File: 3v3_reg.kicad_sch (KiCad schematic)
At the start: 1 part, among them U7 TPS62A01PDDCR

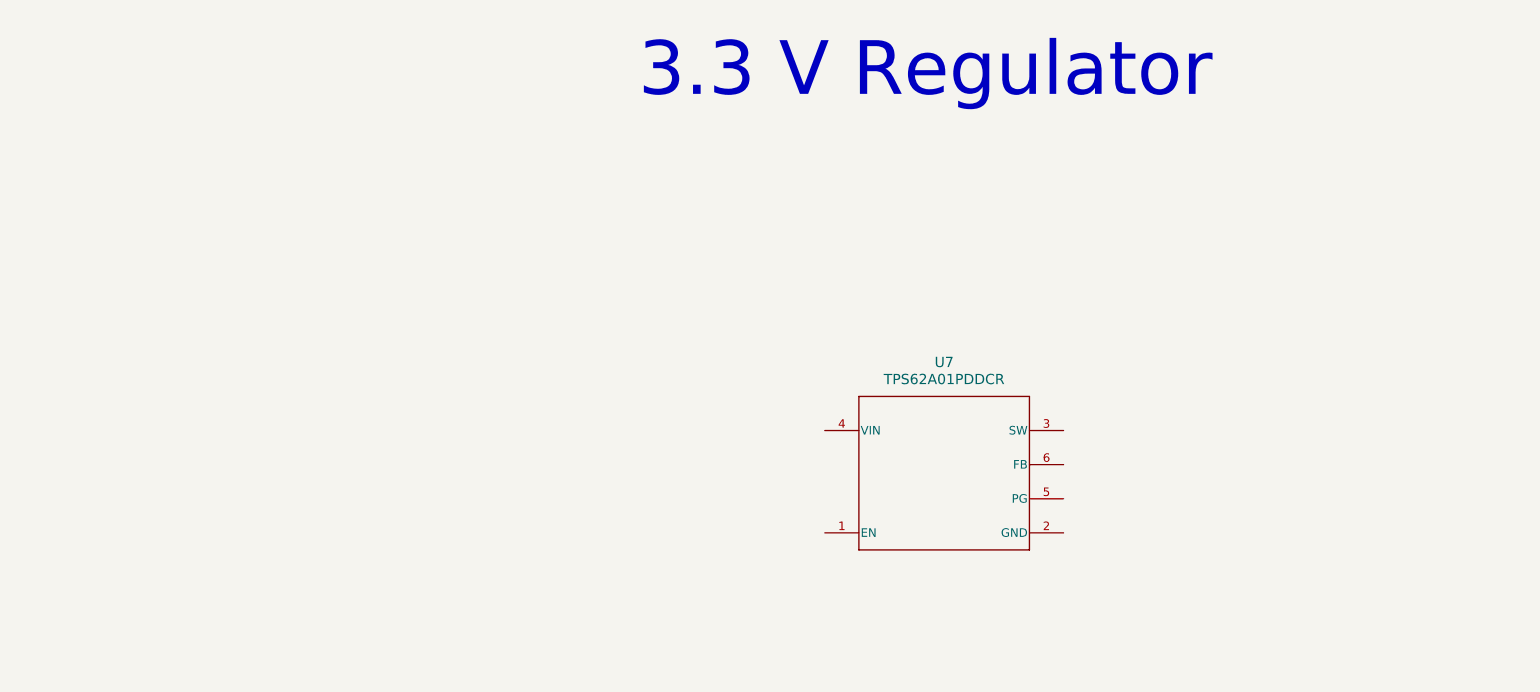
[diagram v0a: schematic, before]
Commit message: did 3v3 reg
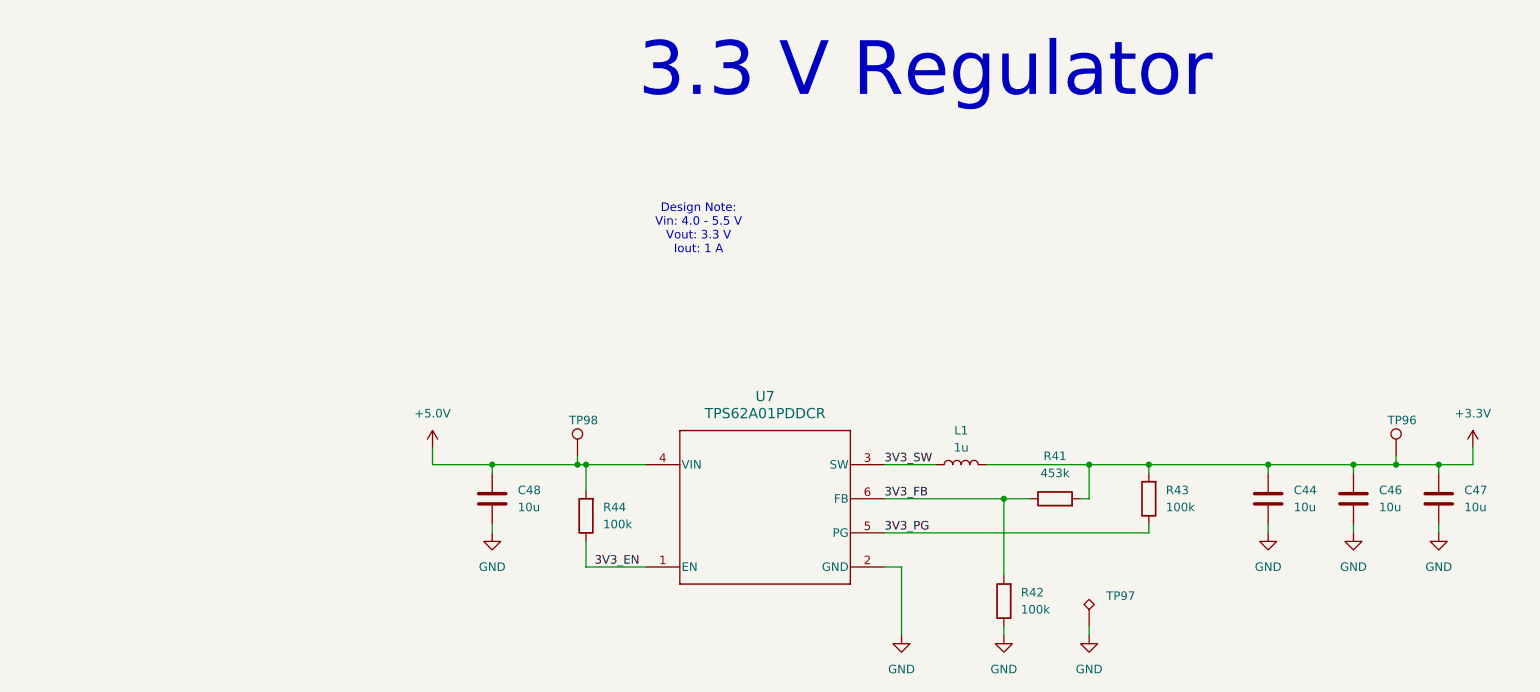
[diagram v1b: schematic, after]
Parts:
- added C44, C46, C47, C48: 10u, Capacitor_SMD:C_0805_2012Metric, symbol Device:C
- added L1: 1u, Inductor_SMD:L_1210_3225Metric, symbol Device:L
- added R41: 453k, Resistor_SMD:R_0402_1005Metric, symbol Device:R
- added R42, R43, R44: 100k, Resistor_SMD:R_0402_1005Metric, symbol Device:R
- added TP96, TP98: TestPoint, symbol Connector:TestPoint
- added TP97: TestPoint_Alt, symbol Connector:TestPoint_Alt
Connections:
- net 3V3_EN: now reaches U7.1 (EN)
- net 3V3_EN: now also R44.1
- net GND: now reaches U7.2 (GND)
- net GND: now also C44.2, C46.2, C47.2, C48.2, R42.1, TP97.1
- net 3V3_SW: now reaches U7.3 (SW)
- net 3V3_SW: now also L1.1
- net +5.0V: now reaches U7.4 (VIN)
- net +5.0V: now also C48.1, R44.2, TP98.1
- net 3V3_PG: now reaches U7.5 (PG)
- net 3V3_PG: now also R43.1
- net 3V3_FB: now reaches U7.6 (FB)
- net 3V3_FB: now also R41.1, R42.2
- new net +3.3V: C44.1, C46.1, C47.1, L1.2, R41.2, R43.2, TP96.1
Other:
- note added: "Design Note: Vin: 4.0 - 5.5 V Vout: 3.3 V Iout: 1 A"
- moved on the sheet: U7

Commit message: did stuff
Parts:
- renumbered C48 to C109, C44 to C110, C46 to C111, C47 to C112, R41 to R80, R43 to R81, R44 to R82, R42 to R83, TP98 to TP133, TP96 to TP134, TP97 to TP135
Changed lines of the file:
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@@
 		(dnp no)
 		(fields_autoplaced yes)
-		(property "Reference" "C44"
+		(property "Reference" "C110"
 			(at 199.39 96.5199 0)
 			(effects
@@
 			(project ""
 				(path "/2970f661-65ab-4e2b-aeda-d76d1044f2b8/4a874178-a54c-4eb4-8350-ff261e3dfdab"
-					(reference "C44")
+					(reference "C110")
 					(unit 1)
 				)
@@
 		(dnp no)
 		(fields_autoplaced yes)
-		(property "Reference" "R44"
+		(property "Reference" "R82"
 			(at 96.52 99.0599 0)
 			(effects
@@
 			(project "netdaq"
 				(path "/2970f661-65ab-4e2b-aeda-d76d1044f2b8/4a874178-a54c-4eb4-8350-ff261e3dfdab"
-					(reference "R44")
+					(reference "R82")
 					(unit 1)
 				)
@@
 		(dnp no)
 		(fields_autoplaced yes)
-		(property "Reference" "#PWR086"
+		(property "Reference" "#PWR0179"
 			(at 226.06 93.98 0)
 			(effects
@@
 			(project ""
 				(path "/2970f661-65ab-4e2b-aeda-d76d1044f2b8/4a874178-a54c-4eb4-8350-ff261e3dfdab"
-					(reference "#PWR086")
+					(reference "#PWR0179")
 					(unit 1)
 				)
@@
 		(dnp no)
 		(fields_autoplaced yes)
-		(property "Reference" "#PWR085"
+		(property "Reference" "#PWR0183"
 			(at 220.98 109.22 0)
 			(effects
@@
 			(project "netdaq"
 				(path "/2970f661-65ab-4e2b-aeda-d76d1044f2b8/4a874178-a54c-4eb4-8350-ff261e3dfdab"
-					(reference "#PWR085")
+					(reference "#PWR0183")
 					(unit 1)
 				)
@@
 		(dnp no)
 		(fields_autoplaced yes)
-		(property "Reference" "#PWR088"
+		(property "Reference" "#PWR0180"
 			(at 80.01 109.22 0)
 			(effects
@@
 			(project "netdaq"
 				(path "/2970f661-65ab-4e2b-aeda-d76d1044f2b8/4a874178-a54c-4eb4-8350-ff261e3dfdab"
-					(reference "#PWR088")
+					(reference "#PWR0180")
 					(unit 1)
 				)
@@
 		(dnp no)
 		(fields_autoplaced yes)
-		(property "Reference" "#PWR089"
+		(property "Reference" "#PWR0178"
 			(at 71.12 93.98 0)
 			(effects
@@
 			(project "netdaq"
 				(path "/2970f661-65ab-4e2b-aeda-d76d1044f2b8/4a874178-a54c-4eb4-8350-ff261e3dfdab"
-					(reference "#PWR089")
+					(reference "#PWR0178")
 					(unit 1)
 				)
@@
 		(dnp no)
 		(fields_autoplaced yes)
-		(property "Reference" "#PWR087"
+		(property "Reference" "#PWR0186"
 			(at 168.91 124.46 0)
 			(effects
@@
 			(project "netdaq"
 				(path "/2970f661-65ab-4e2b-aeda-d76d1044f2b8/4a874178-a54c-4eb4-8350-ff261e3dfdab"
-					(reference "#PWR087")
+					(reference "#PWR0186")
 					(unit 1)
 				)
@@
 		(on_board yes)
 		(dnp no)
-		(property "Reference" "TP98"
+		(property "Reference" "TP133"
 			(at 91.44 86.106 0)
 			(effects
@@
 			(project "netdaq"
 				(path "/2970f661-65ab-4e2b-aeda-d76d1044f2b8/4a874178-a54c-4eb4-8350-ff261e3dfdab"
-					(reference "TP98")
+					(reference "TP133")
 					(unit 1)
 				)
@@
 		(dnp no)
 		(fields_autoplaced yes)
-		(property "Reference" "#PWR082"
+		(property "Reference" "#PWR0185"
 			(at 156.21 124.46 0)
 			(effects
@@
 			(project "netdaq"
 				(path "/2970f661-65ab-4e2b-aeda-d76d1044f2b8/4a874178-a54c-4eb4-8350-ff261e3dfdab"
-					(reference "#PWR082")
+					(reference "#PWR0185")
 					(unit 1)
 				)
@@
 		(dnp no)
 		(fields_autoplaced yes)
-		(property "Reference" "#PWR081"
+		(property "Reference" "#PWR0184"
 			(at 140.97 124.46 0)
 			(effects
@@
 			(project ""
 				(path "/2970f661-65ab-4e2b-aeda-d76d1044f2b8/4a874178-a54c-4eb4-8350-ff261e3dfdab"
-					(reference "#PWR081")
+					(reference "#PWR0184")
 					(unit 1)
 				)
@@
 		(dnp no)
 		(fields_autoplaced yes)
-		(property "Reference" "C46"
+		(property "Reference" "C111"
 			(at 212.09 96.5199 0)
 			(effects
@@
 			(project "netdaq"
 				(path "/2970f661-65ab-4e2b-aeda-d76d1044f2b8/4a874178-a54c-4eb4-8350-ff261e3dfdab"
-					(reference "C46")
+					(reference "C111")
 					(unit 1)
 				)
@@
 		(dnp no)
 		(fields_autoplaced yes)
-		(property "Reference" "#PWR084"
+		(property "Reference" "#PWR0182"
 			(at 208.28 109.22 0)
 			(effects
@@
 			(project "netdaq"
 				(path "/2970f661-65ab-4e2b-aeda-d76d1044f2b8/4a874178-a54c-4eb4-8350-ff261e3dfdab"
-					(reference "#PWR084")
+					(reference "#PWR0182")
 					(unit 1)
 				)
@@
 		(on_board yes)
 		(dnp no)
-		(property "Reference" "TP96"
+		(property "Reference" "TP134"
 			(at 213.36 86.106 0)
 			(effects
@@
 			(project "netdaq"
 				(path "/2970f661-65ab-4e2b-aeda-d76d1044f2b8/4a874178-a54c-4eb4-8350-ff261e3dfdab"
-					(reference "TP96")
+					(reference "TP134")
 					(unit 1)
 				)
@@
 		(dnp no)
 		(fields_autoplaced yes)
-		(property "Reference" "R41"
+		(property "Reference" "R80"
 			(at 163.83 91.44 90)
 			(effects
@@
 			(project ""
 				(path "/2970f661-65ab-4e2b-aeda-d76d1044f2b8/4a874178-a54c-4eb4-8350-ff261e3dfdab"
-					(reference "R41")
+					(reference "R80")
 					(unit 1)
 				)
@@
 		(dnp no)
 		(fields_autoplaced yes)
-		(property "Reference" "R43"
+		(property "Reference" "R81"
 			(at 180.34 96.5199 0)
 			(effects
@@
 			(project "netdaq"
 				(path "/2970f661-65ab-4e2b-aeda-d76d1044f2b8/4a874178-a54c-4eb4-8350-ff261e3dfdab"
-					(reference "R43")
+					(reference "R81")
 					(unit 1)
 				)
@@
 		(dnp no)
 		(fields_autoplaced yes)
-		(property "Reference" "R42"
+		(property "Reference" "R83"
 			(at 158.75 111.7599 0)
 			(effects
@@
 			(project "netdaq"
 				(path "/2970f661-65ab-4e2b-aeda-d76d1044f2b8/4a874178-a54c-4eb4-8350-ff261e3dfdab"
-					(reference "R42")
+					(reference "R83")
 					(unit 1)
 				)
@@
 		(dnp no)
 		(fields_autoplaced yes)
-		(property "Reference" "TP97"
+		(property "Reference" "TP135"
 			(at 171.45 112.2679 0)
 			(effects
@@
 			(project "netdaq"
 				(path "/2970f661-65ab-4e2b-aeda-d76d1044f2b8/4a874178-a54c-4eb4-8350-ff261e3dfdab"
-					(reference "TP97")
+					(reference "TP135")
 					(unit 1)
 				)
@@
 		(dnp no)
 		(fields_autoplaced yes)
-		(property "Reference" "C47"
+		(property "Reference" "C112"
 			(at 224.79 96.5199 0)
 			(effects
@@
 			(project "netdaq"
 				(path "/2970f661-65ab-4e2b-aeda-d76d1044f2b8/4a874178-a54c-4eb4-8350-ff261e3dfdab"
-					(reference "C47")
+					(reference "C112")
 					(unit 1)
 				)
@@
 		(dnp no)
 		(fields_autoplaced yes)
-		(property "Reference" "C48"
+		(property "Reference" "C109"
 			(at 83.82 96.5199 0)
 			(effects
@@
 			(project "netdaq"
 				(path "/2970f661-65ab-4e2b-aeda-d76d1044f2b8/4a874178-a54c-4eb4-8350-ff261e3dfdab"
-					(reference "C48")
+					(reference "C109")
 					(unit 1)
 				)
@@
 		(dnp no)
 		(fields_autoplaced yes)
-		(property "Reference" "#PWR083"
+		(property "Reference" "#PWR0181"
 			(at 195.58 109.22 0)
 			(effects
@@
 			(project "netdaq"
 				(path "/2970f661-65ab-4e2b-aeda-d76d1044f2b8/4a874178-a54c-4eb4-8350-ff261e3dfdab"
-					(reference "#PWR083")
-					(unit 1)
-				)
+					(reference "#PWR0181")
+					(unit 1)
+				)

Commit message: changed to 4 layer, finished usb conn, added jtag conn, some other things
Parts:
- TP133, TP134: footprint (none) -> TestPoint:TestPoint_THTPad_D1.0mm_Drill0.5mm
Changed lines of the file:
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@@
 			)
 		)
-		(property "Footprint" ""
+		(property "Footprint" "TestPoint:TestPoint_THTPad_D1.0mm_Drill0.5mm"
 			(at 97.79 91.44 0)
 			(hide yes)
@@
 			)
 		)
-		(property "Footprint" ""
+		(property "Footprint" "TestPoint:TestPoint_THTPad_D1.0mm_Drill0.5mm"
 			(at 219.71 91.44 0)
 			(hide yes)

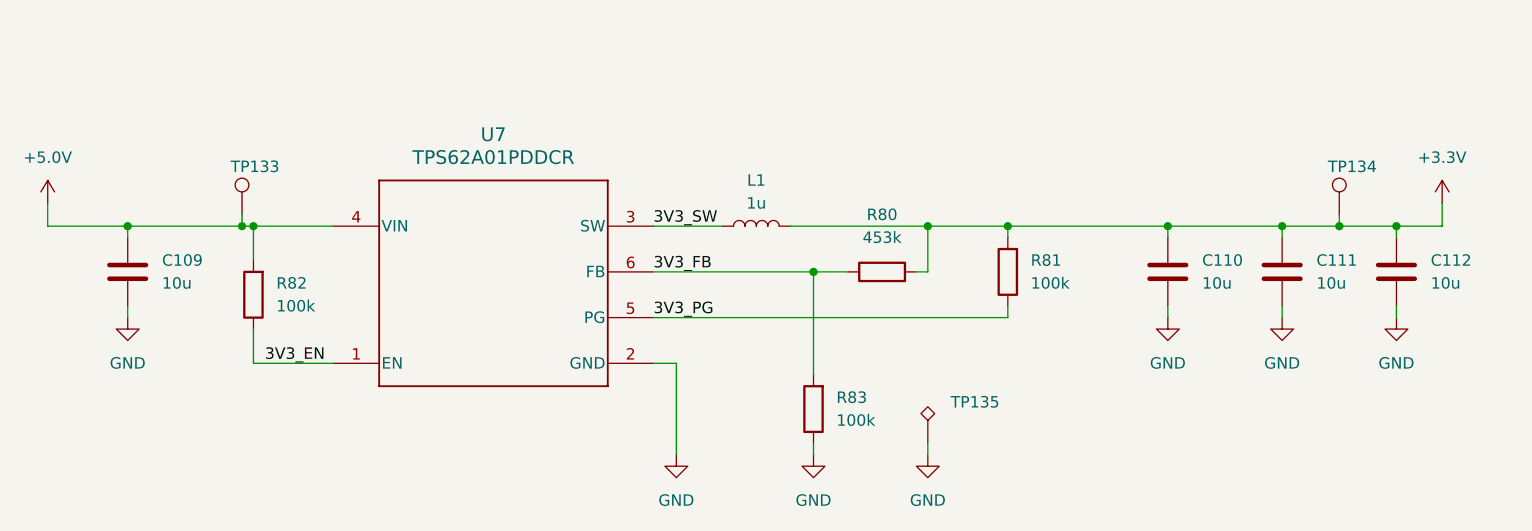
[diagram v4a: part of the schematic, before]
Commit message: did a bunch of bom matching to lcsc
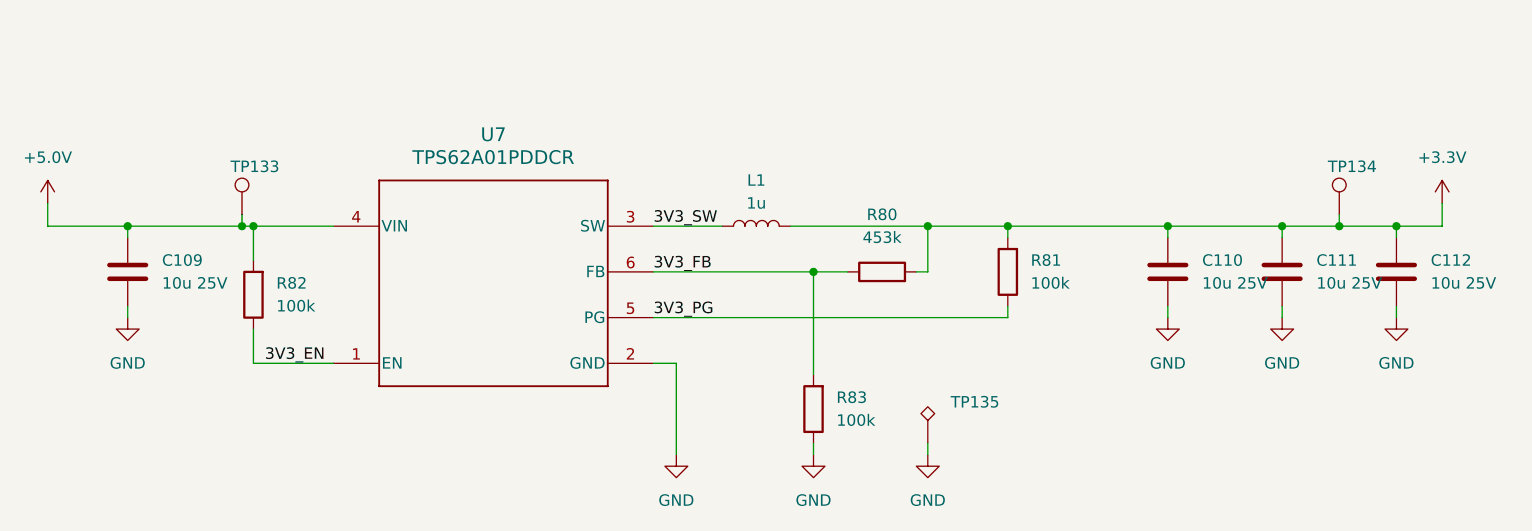
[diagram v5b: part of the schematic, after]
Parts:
- C109, C110, C111, C112: value 10u -> 10u 25V; LCSC (none) -> C15850; LCSC Basic/Pref (none) -> x; LCSC Part (none) -> C15850
- R80: LCSC Basic/Pref (none) -> n
- R81, R82, R83: LCSC (none) -> C25741; LCSC Basic/Pref (none) -> x; LCSC Part (none) -> C25741
- TP133, TP134: now left out of the parts list
- TP135: footprint (none) -> TestPoint:TestPoint_THTPad_1.0x1.0mm_Drill0.5mm; now left out of the parts list
- U7: LCSC Part (none) -> C42267816

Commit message: did almost nothing!
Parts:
- added D79, D81: D_Schottky, Diode_SMD:D_SOD-323, symbol Device:D_Schottky
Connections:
- net +5.0V: now also D81.2 (A); no longer C109.1, R82.2, TP133.1, U7.4 (VIN)
- new net: C109.1, D79.1 (K), D81.1 (K), R82.2, TP133.1, U7.4 (VIN)
- new net +5.2V: D79.2 (A)
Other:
- note added: "todo: change to C146335"
- note added: "todo: there are preferred diodes, can we change"

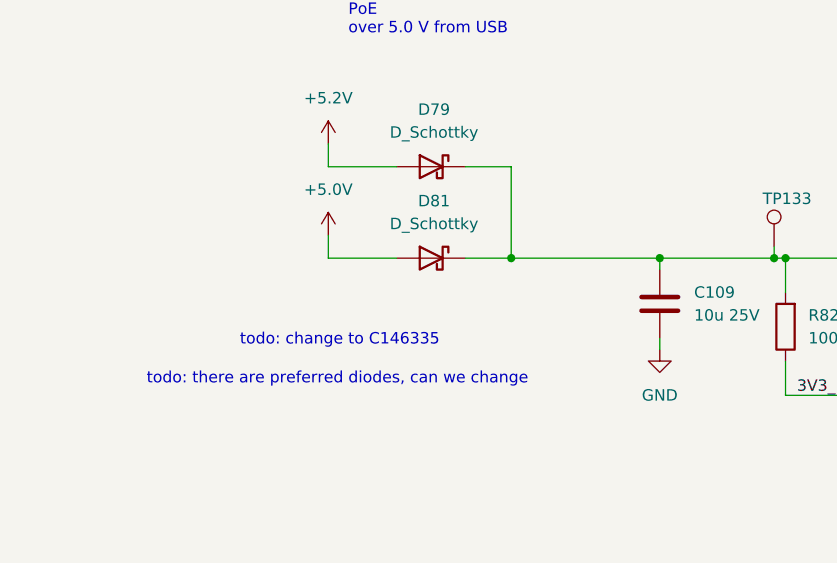
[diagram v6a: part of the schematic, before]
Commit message: did some ethernet, found preferred power switch diode
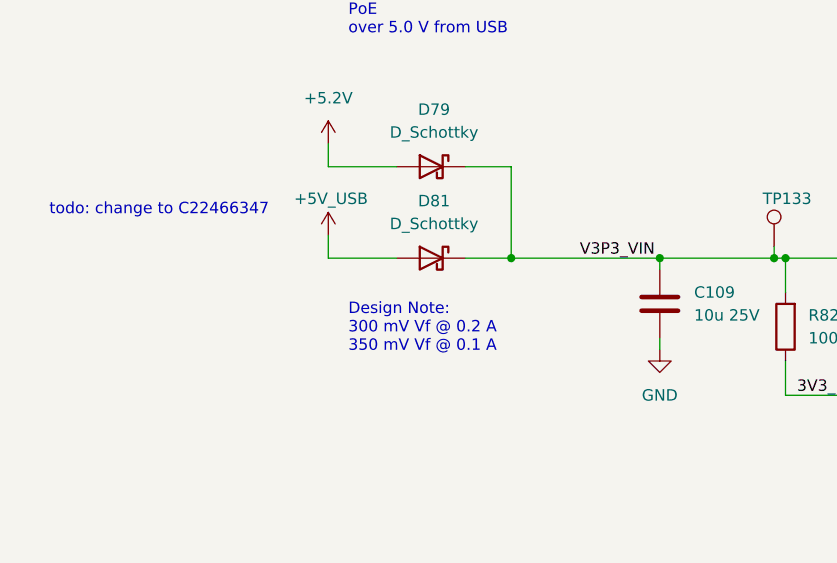
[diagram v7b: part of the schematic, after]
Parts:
- D79, D81: footprint Diode_SMD:D_SOD-323 -> Diode_SMD:D_SOD-123F
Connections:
- net V3P3_VIN: now reaches C109.1, D79.1 (K), D81.1 (K), R82.2, TP133.1, U7.4 (VIN)
- net +5.0V renamed +5V_USB
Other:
- note added: "todo: change to C22466347"
- note removed: "todo: change to C146335"
- note removed: "todo: there are preferred diodes, can we change"
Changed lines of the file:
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@@
 	(generator_version "10.0")
 	(paper "A4")
-	(text "todo: there are preferred diodes, can we change"
+	(text "todo: change to C22466347"
 		(exclude_from_sim no)
-		(at 44.196 106.172 0)
-		(effects
-			(font
-				(size 1.27 1.27)
-			)
-		)
-	)
-	(text "todo: change to C146335"
-		(exclude_from_sim no)
-		(at 44.45 101.854 0)
+		(at 24.384 87.376 0)
 		(effects
 			(font
@@
 		)
 	)
+	(text_box "Design Note:\n300 mV Vf @ 0.2 A\n350 mV Vf @ 0.1 A"
+		(exclude_from_sim no)
+		(at 44.45 96.52 0)
+		(size 22.86 12.7)
+		(margins 0.9525 0.9525 0.9525 0.9525)
+		(stroke
+			(width -0.0001)
+			(type solid)
+		)
+		(fill
+			(type none)
+		)
+		(effects
+			(font
+				(size 1.27 1.27)
+			)
+			(justify left top)
+		)
+	)
 	(junction
 		(at 63.5 92.71)
@@
 	(label "3V3_SW"
 		(at 138.43 92.71 0)
+		(effects
+			(font
+				(size 1.27 1.27)
+			)
+			(justify left bottom)
+		)
+	)
+	(label "V3P3_VIN"
+		(at 71.12 92.71 0)
 		(effects
 			(font
@@
 			)
 		)
-		(property "Footprint" "Diode_SMD:D_SOD-323"
+		(property "Footprint" "Diode_SMD:D_SOD-123F"
 			(at 54.61 82.55 0)
 			(hide yes)
@@
 			)
 		)
-		(property "Footprint" "Diode_SMD:D_SOD-323"
+		(property "Footprint" "Diode_SMD:D_SOD-123F"
 			(at 54.61 92.71 0)
 			(hide yes)
@@
 		(in_pos_files yes)
 		(dnp no)
-		(fields_autoplaced yes)
 		(property "Reference" "#PWR0178"
 			(at 43.18 93.98 0)
@@
 			)
 		)
-		(property "Value" "+5.0V"
-			(at 43.18 85.09 0)
-			(show_name no)
-			(do_not_autoplace no)
-			(effects
-				(font
-					(size 1.27 1.27)
-				)
-			)
-		)
+		(property "Value" "+5V_USB"
+			(at 39.37 86.106 0)
+			(show_name no)
+			(do_not_autoplace no)
+			(effects
+				(font
+					(size 1.27 1.27)
+				)
+				(justify left)
+			)
+		)

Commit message: bunch of stuff
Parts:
- R80: value 453k -> 300k; footprint Resistor_SMD:R_0402_1005Metric -> Resistor_SMD:R_0603_1608Metric; LCSC (none) -> C23024; LCSC Basic/Pref n -> x; LCSC Part (none) -> C23024
- R83: value 100k -> 68k; footprint Resistor_SMD:R_0402_1005Metric -> Resistor_SMD:R_0603_1608Metric; LCSC C25741 -> C23231; LCSC Part C25741 -> C23231
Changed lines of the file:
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@@
 			)
 		)
-		(property "Value" "453k"
+		(property "Value" "300k"
 			(at 163.83 93.98 90)
 			(show_name no)
@@
 			)
 		)
-		(property "Footprint" "Resistor_SMD:R_0402_1005Metric"
+		(property "Footprint" "Resistor_SMD:R_0603_1608Metric"
 			(at 163.83 99.568 90)
 			(hide yes)
@@
 			)
 		)
-		(property "LCSC Basic/Pref" "n"
+		(property "LCSC Basic/Pref" "x"
 			(at 163.83 97.79 90)
 			(hide yes)
@@
 		)
 		(property "LCSC missing" ""
+			(at 163.83 97.79 90)
+			(hide yes)
+			(show_name no)
+			(do_not_autoplace no)
+			(effects
+				(font
+					(size 1.27 1.27)
+				)
+			)
+		)
+		(property "LCSC" "C23024"
+			(at 163.83 97.79 90)
+			(hide yes)
+			(show_name no)
+			(do_not_autoplace no)
+			(effects
+				(font
+					(size 1.27 1.27)
+				)
+			)
+		)
+		(property "LCSC Part" "C23024"
 			(at 163.83 97.79 90)
 			(hide yes)
@@
 			)
 		)
-		(property "Value" "100k"
+		(property "Value" "68k"
 			(at 158.75 114.2999 0)
 			(show_name no)
@@
 			)
 		)
-		(property "Footprint" "Resistor_SMD:R_0402_1005Metric"
+		(property "Footprint" "Resistor_SMD:R_0603_1608Metric"
 			(at 157.988 113.03 90)
 			(hide yes)
@@
 			)
 		)
-		(property "LCSC" "C25741"
+		(property "LCSC" "C23231"
 			(at 156.21 113.03 0)
 			(hide yes)
@@
 			)
 		)
-		(property "LCSC Part" "C25741"
+		(property "LCSC Part" "C23231"
 			(at 156.21 113.03 0)
 			(hide yes)
